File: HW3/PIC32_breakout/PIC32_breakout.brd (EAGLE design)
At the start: 50 x 50 mm, 24 parts

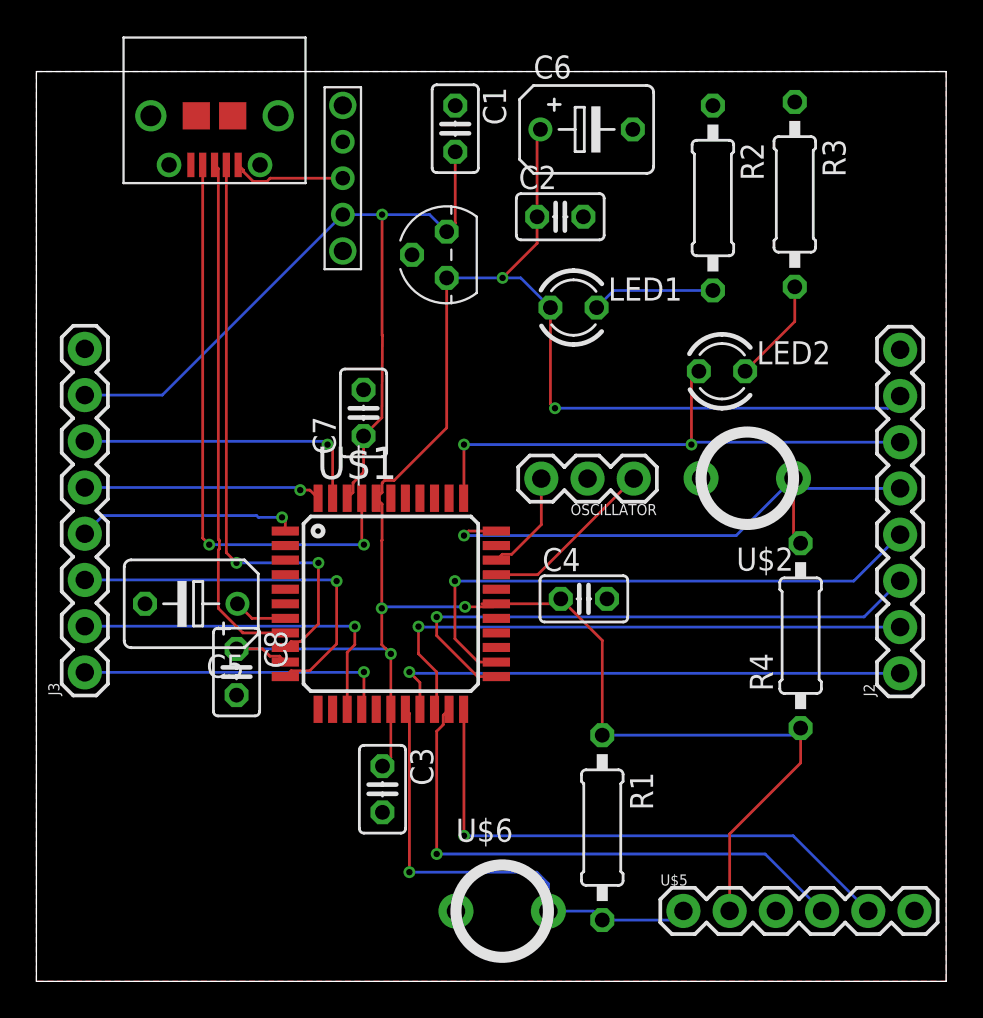
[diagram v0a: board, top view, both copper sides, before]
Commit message: checked board CAM
added mounting holes and checked CAM files against Seeed. They let me add to cart so I'll assume it's fine.
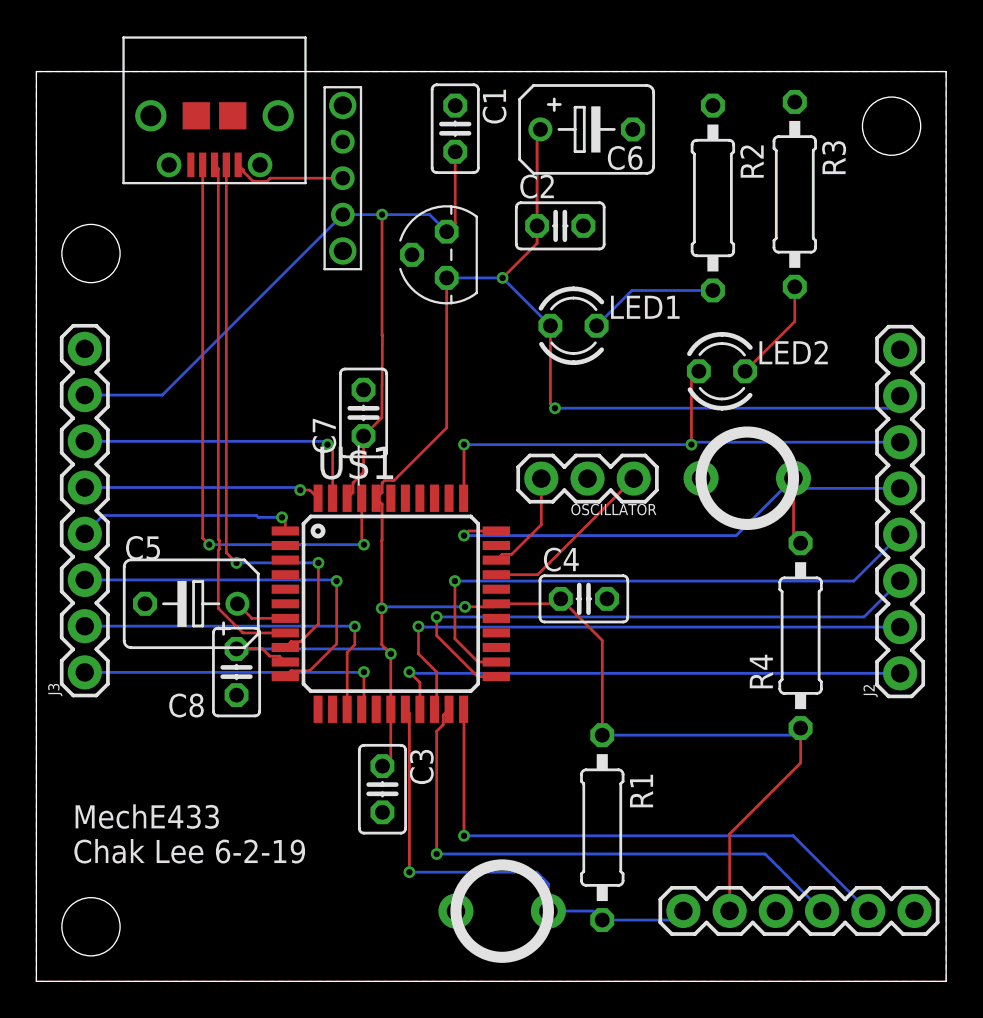
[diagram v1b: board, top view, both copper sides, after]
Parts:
- U$2: value SWITCH_BTN_NO -> USER
- U$6: value SWITCH_BTN_NO -> RESET
- moved LED1 1.00 mm to (29.5, 36.0)
- moved C2 0.50 mm to (28.8, 41.5)
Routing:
- net +3V3: track 123.1 -> 121.8 mm
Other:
- board text added: "MechE433 Chak Lee 6-2-19"
